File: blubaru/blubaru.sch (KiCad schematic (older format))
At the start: 2 parts, among them J3 DB15, J5 DB15

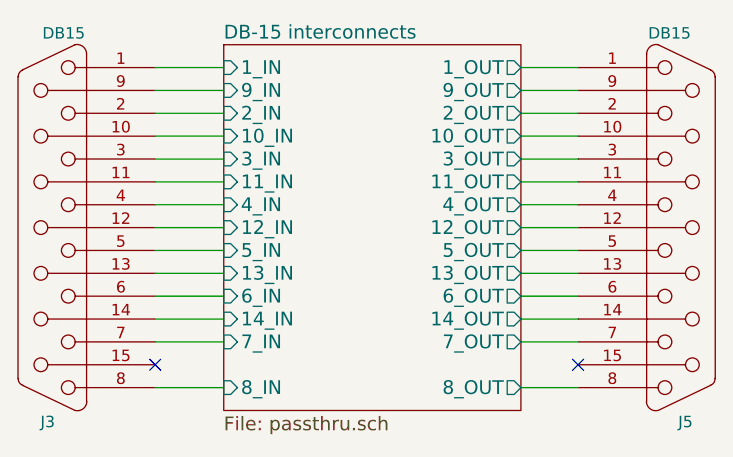
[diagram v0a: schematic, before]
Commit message: Put parts in the audio switch page.
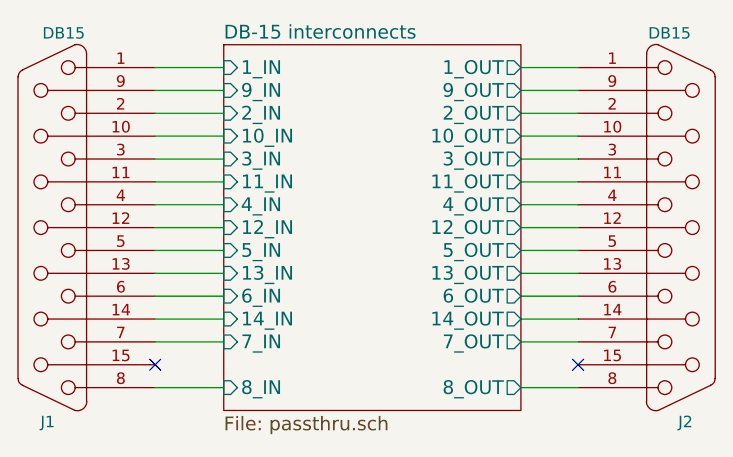
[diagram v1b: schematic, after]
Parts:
- renumbered J3 to J1, J5 to J2
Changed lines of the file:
@@
 $EndDescr
 $Comp
-L DB15 J5
+L DB15 J2
 U 1 1 589BBD0D
 P 6850 4000
-F 0 "J5" H 6870 4850 50  0000 C CNN
+F 0 "J2" H 6870 4850 50  0000 C CNN
 F 1 "DB15" H 6800 3150 50  0000 C CNN
 F 2 "" H 6850 4000 50  0000 C CNN
@@
 $EndComp
 $Comp
-L DB15 J3
+L DB15 J1
 U 1 1 589BBD68
 P 4100 4000
-F 0 "J3" H 4120 4850 50  0000 C CNN
+F 0 "J1" H 4120 4850 50  0000 C CNN
 F 1 "DB15" H 4050 3150 50  0000 C CNN
 F 2 "" H 4100 4000 50  0000 C CNN

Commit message: Create footprints for breakout boards
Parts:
- J1: footprint (none) -> Connectors:DB15FC
- J2: footprint (none) -> Connectors:DB15MC
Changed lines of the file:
@@
 encoding utf-8
 Sheet 1 8
-Title ""
-Date ""
-Rev ""
+Title "Blubaru"
+Date "2017-02-28"
+Rev "0.1"
 Comp ""
 Comment1 ""
@@
 F 0 "J2" H 6870 4850 50  0000 C CNN
 F 1 "DB15" H 6800 3150 50  0000 C CNN
-F 2 "" H 6850 4000 50  0000 C CNN
+F 2 "Connectors:DB15MC" H 6850 4000 50  0001 C CNN
 F 3 "" H 6850 4000 50  0000 C CNN
 	1    6850 4000
@@
 F 0 "J1" H 4120 4850 50  0000 C CNN
 F 1 "DB15" H 4050 3150 50  0000 C CNN
-F 2 "" H 4100 4000 50  0000 C CNN
+F 2 "Connectors:DB15FC" H 4100 4000 50  0001 C CNN
 F 3 "" H 4100 4000 50  0000 C CNN
 	1    4100 4000
